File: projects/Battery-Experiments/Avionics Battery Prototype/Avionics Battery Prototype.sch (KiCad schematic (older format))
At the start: 21 parts, among them U1 LM324A

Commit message: AVB Start
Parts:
- removed U1: LM324A, symbol Amplifier_Operational:LM324A
- added C1, C2, C3, C4: 0.1u, Capacitors_SMD:C_1206_HandSoldering, symbol Device:C
- added C5, C6: 1u, Capacitors_SMD:C_1206_HandSoldering, symbol Device:C
- added C7, C9: 10n, Capacitors_SMD:C_1206_HandSoldering, symbol Device:C
- added C8: 10u, Capacitors_SMD:C_1206_HandSoldering, symbol Device:C
- added D1, D2, D3, D4: 3.6V Zener, Diodes_SMD:D_SOD-123F, symbol Device:D_Zener_ALT
- added D5, D6: LED, LEDs:LED_1206_HandSoldering, symbol Device:LED_ALT
- added J1: Jack-DC, Connect:Banana_Jack_2Pin, symbol Connector:Jack-DC
- added J2: TP, Pin_Headers:Pin_Header_Straight_1x02_Pitch2.54mm, symbol Connector_Generic:Conn_01x02
- added J3: UART, Pin_Headers:Pin_Header_Straight_1x03_Pitch2.54mm, symbol Connector_Generic:Conn_01x03
- added J4: SBW JTAG, Pin_Headers:Pin_Header_Straight_1x06_Pitch2.54mm, symbol Connector_Generic:Conn_01x06
- added R10, R15, R20, R23, R24, R5: 330, Resistors_SMD:R_1206_HandSoldering, symbol Device:R
- added R21, R22, R25: 33k, Resistors_SMD:R_1206_HandSoldering, symbol Device:R
- added U1, U2: OPA4197, SMD_Packages:SOIC-14_N, symbol k7arx:OPA4322
- added U3: CD4052B, SMD_Packages:SO-16-N, symbol Analog_Switch:CD4052B
- added U4: LT1763, SMD_Packages:SOIC-8-N, symbol k7arx:LT1763
- added U5: MSP430G2233, SMD_Packages:SSOP-20, symbol k7arx:MSP430G2233
- added U6: CD40109B, SMD_Packages:SO-16-N, symbol k7arx:CD40109B
- BT1, BT2, BT3, BT4: value Battery_Cell -> 14430; footprint (none) -> k7arx:Keystone-92 Battery_Contact 14430
- R1, R2: value 20k -> 200k; footprint (none) -> Resistors_SMD:R_1206_HandSoldering
- R11: renamed from R9; value 20k -> 200k; footprint (none) -> Resistors_SMD:R_1206_HandSoldering
- R12: renamed from R10; value 20k -> 200k; footprint (none) -> Resistors_SMD:R_1206_HandSoldering
- R13: renamed from R11; value 10k -> 100k; footprint (none) -> Resistors_SMD:R_1206_HandSoldering
- R14: renamed from R12; value 10k -> 100k; footprint (none) -> Resistors_SMD:R_1206_HandSoldering
- R16: renamed from R13; value 20k -> 200k; footprint (none) -> Resistors_SMD:R_1206_HandSoldering
- R17: renamed from R14; value 20k -> 200k; footprint (none) -> Resistors_SMD:R_1206_HandSoldering
- R18: renamed from R15; value 10k -> 100k; footprint (none) -> Resistors_SMD:R_1206_HandSoldering
- R19: renamed from R16; value 10k -> 100k; footprint (none) -> Resistors_SMD:R_1206_HandSoldering
- R3, R4: value 10k -> 100k; footprint (none) -> Resistors_SMD:R_1206_HandSoldering
- R6: renamed from R5; value 20k -> 200k; footprint (none) -> Resistors_SMD:R_1206_HandSoldering
- R7: renamed from R6; value 20k -> 200k; footprint (none) -> Resistors_SMD:R_1206_HandSoldering
- R8: renamed from R7; value 10k -> 100k; footprint (none) -> Resistors_SMD:R_1206_HandSoldering
- R9: renamed from R8; value 10k -> 100k; footprint (none) -> Resistors_SMD:R_1206_HandSoldering
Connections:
- net +BATT: now also C6.1, J2.2 (Pin_2), R21.1, U1.10 (+), U1.4 (V+), U2.4 (V+), U3.16 (VDD), U4.5 (~SHDN), U4.8 (VIN), U6.16 (Vdd); no longer BT4.1 (+), R17.2
- net GND: now also C1.2, C2.2, C3.2, C4.2, C6.2, C8.2, C9.2, D1.2 (A), D2.2 (A), D3.2 (A), D4.2 (A), D5.1 (K), D6.1 (K), J1.2, J3.1 (Pin_1), J4.3 (Pin_3), J4.5 (Pin_5), R25.2, U1.11 (V-), U2.11 (V-), U3.1 (Y0), U3.7 (VEE), U3.8 (VSS), U4.3 (GND), U4.6 (GND), U4.7 (GND), U5.14 (P1.6), U5.15 (P1.7), U5.18 (XOut), U5.19 (XIn), U5.20 (DVss), U6.13 (H), U6.14 (D), U6.15 (En_D), U6.8 (Vss)
- net V1: now also C1.1, D1.1 (K), R5.1, U5.2 (P1.0); no longer R3.1
- net V2: now also C2.1, D2.1 (K), R10.1, U5.3 (P1.1); no longer R8.1
- net V3: now also C3.1, D3.1 (K), R15.1, U5.4 (P1.2); no longer R13.1
- net V4: now also C4.1, D4.1 (K), R20.1, U5.5 (P1.3); no longer R18.1
- net at BT3.1 (+), BT4.2 (-): now also U1.12 (+), U3.15 (X2), U3.4 (Y3); no longer R12.2, R16.2
- net at BT2.1 (+), BT3.2 (-): now also U1.5 (+), U3.14 (X1), U3.2 (Y2); no longer R11.2, R7.2
- net at BT1.1 (+), BT2.2 (-): now also U1.3 (+), U3.12 (X0), U3.5 (Y1); no longer R2.2, R6.2
- net at R1.1, R3.2: now also U2.2 (-)
- net at R2.1, R4.2: now also U2.3 (+)
- net at R7.1, R9.2: now also U2.5 (+)
- net at R6.1, R8.2: now also U2.6 (-)
- net at R12.1, R14.2: now also U2.10 (+)
- net at R11.1, R13.2: now also U2.9 (-)
- net at R17.1, R19.2: now also U2.12 (+)
- net at R16.1, R18.2: now also U2.13 (-)
- new net: BT4.1 (+), J1.1, J2.1 (Pin_1), U3.11 (X3)
- new net: R2.2, R6.2, U1.1, U1.2 (-)
- new net: R11.2, R7.2, U1.6 (-), U1.7
- new net: R12.2, R16.2, U1.13 (-), U1.14
- new net: R17.2, U1.8, U1.9 (-)
- new net: C5.1, U3.13 (X)
- new net: C5.2, U3.3 (Y)
- new net: U3.10 (A), U6.4 (E)
- new net: R21.2, U3.6 (INH), U6.11 (G)
- new net: U3.9 (B), U6.5 (F)
- new net: R3.1, R5.2, U2.1
- new net: R10.2, R8.1, U2.7
- new net: R13.1, R15.2, U2.8
- new net: R18.1, R20.2, U2.14
- new net: C7.2, U4.4 (BYP)
- new net: U5.10 (P2.2), U6.10 (C)
- new net: R25.1, U5.11 (P2.3), U6.2 (En_A), U6.7 (En_B), U6.9 (En_C)
- new net: U5.8 (P2.0), U6.3 (A)
- new net: U5.9 (P2.1), U6.6 (B)
- new net: R23.1, U5.6 (P1.4)
- new net: D5.2 (A), R23.2
- new net: R24.1, U5.7 (P1.5)
- new net: D6.2 (A), R24.2
- new net +3V3: C7.1, C8.1, J4.2 (Pin_2), J4.4 (Pin_4), R22.1, U4.1 (VOUT), U4.2 (SENSE), U5.1 (DVcc), U6.1 (Vcc)
- new net TEST: J4.6 (Pin_6), U5.17 (TEST)
- new net UART_RX: J3.2 (Pin_2), U5.12 (P2.4)
- new net UART_TX: J3.3 (Pin_3), U5.13 (P2.5)
- new net ~RST: C9.1, J4.1 (Pin_1), R22.2, U5.16 (~RST)
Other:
- note added: "Battery balancing and monitoring circuit"
- note added: "Battery control system circuit"
- moved on the sheet: BT1, BT2, BT3, BT4, R1, R11, R12, R13, R14, R16, R17, R18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

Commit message: AVB Rev B Complete
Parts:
- added S1: Power Switch, k7arx:PB400 DPST Pushbutton Switch, symbol k7arx:DPST_PowerSwitch
- added S2: Tac Switch, k7arx:EVQ2_Momentary_Switch, symbol k7arx:TactileSwitch_NO
- added TP1: 3V3, Pin_Headers:Pin_Header_Straight_1x01_Pitch2.54mm, symbol Connector:Conn_01x01_Female
- added TP2: Gnd, Pin_Headers:Pin_Header_Straight_1x01_Pitch2.54mm, symbol Connector:Conn_01x01_Female
- J2: value TP -> Enable
- J4: footprint Pin_Headers:Pin_Header_Straight_1x06_Pitch2.54mm -> k7arx:Tag-Connect_TC2030-NL
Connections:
- net +3V3: now also TP1.1 (Pin_1)
- net GND: now also S2.2 (COM), TP2.1 (Pin_1)
- net ~RST: now also S2.1 (NO)
- net at BT4.1 (+), U3.11 (X3): now also S1.2 (COM1), S1.4 (COM2); no longer J1.1, J2.1 (Pin_1)
- new net: J1.1, J2.1 (Pin_1), S1.1 (NO1), S1.3 (NO2)
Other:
- moved on the sheet: C9, J1, J2, R22
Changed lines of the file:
@@
 L Device:R R22
 U 1 1 605F86BF
-P 3650 2750
-F 0 "R22" H 3720 2796 50  0000 L CNN
-F 1 "33k" V 3650 2675 50  0000 L CNN
-F 2 "Resistors_SMD:R_1206_HandSoldering" V 3580 2750 50  0001 C CNN
-F 3 "~" H 3650 2750 50  0001 C CNN
-	1    3650 2750
+P 3350 2750
+F 0 "R22" H 3420 2796 50  0000 L CNN
+F 1 "33k" V 3350 2675 50  0000 L CNN
+F 2 "Resistors_SMD:R_1206_HandSoldering" V 3280 2750 50  0001 C CNN
+F 3 "~" H 3350 2750 50  0001 C CNN
+	1    3350 2750
 	1    0    0    -1
 $EndComp
@@
 L Device:C C9
 U 1 1 605F8EF7
-P 3650 3250
-F 0 "C9" H 3765 3296 50  0000 L CNN
-F 1 "10n" H 3765 3205 50  0000 L CNN
-F 2 "Capacitors_SMD:C_1206_HandSoldering" H 3688 3100 50  0001 C CNN
-F 3 "~" H 3650 3250 50  0001 C CNN
-	1    3650 3250
+P 3350 3250
+F 0 "C9" H 3465 3296 50  0000 L CNN
+F 1 "10n" H 3465 3205 50  0000 L CNN
+F 2 "Capacitors_SMD:C_1206_HandSoldering" H 3388 3100 50  0001 C CNN
+F 3 "~" H 3350 3250 50  0001 C CNN
+	1    3350 3250
 	1    0    0    -1
 $EndComp
@@
 L power:GND #PWR0118
 U 1 1 605F9538
-P 3650 3450
-F 0 "#PWR0118" H 3650 3200 50  0001 C CNN
-F 1 "GND" H 3650 3300 50  0000 C CNN
-F 2 "" H 3650 3450 50  0001 C CNN
-F 3 "" H 3650 3450 50  0001 C CNN
-	1    3650 3450
-	1    0    0    -1
-$EndComp
-Text GLabel 3750 3000 2    50   Input ~ 0
+P 3350 3450
+F 0 "#PWR0118" H 3350 3200 50  0001 C CNN
+F 1 "GND" H 3350 3300 50  0000 C CNN
+F 2 "" H 3350 3450 50  0001 C CNN
+F 3 "" H 3350 3450 50  0001 C CNN
+	1    3350 3450
+	1    0    0    -1
+$EndComp
+Text GLabel 3900 3000 2    50   Input ~ 0
 ~RST
 Text GLabel 2850 2900 2    50   Input ~ 0
@@
 L Connector:Jack-DC J1
 U 1 1 6078A590
-P 6050 1200
-F 0 "J1" H 6107 1525 50  0000 C CNN
-F 1 "Jack-DC" H 6107 1434 50  0000 C CNN
-F 2 "Connect:Banana_Jack_2Pin" H 6100 1160 50  0001 C CNN
-F 3 "~" H 6100 1160 50  0001 C CNN
-	1    6050 1200
+P 5700 1200
+F 0 "J1" H 5757 1525 50  0000 C CNN
+F 1 "Jack-DC" H 5757 1434 50  0000 C CNN
+F 2 "Connect:Banana_Jack_2Pin" H 5750 1160 50  0001 C CNN
+F 3 "~" H 5750 1160 50  0001 C CNN
+	1    5700 1200
 	1    0    0    -1
 $EndComp
@@
 L power:GND #PWR0124
 U 1 1 607952FC
-P 6400 1350
-F 0 "#PWR0124" H 6400 1100 50  0001 C CNN
-F 1 "GND" H 6400 1200 50  0000 C CNN
-F 2 "" H 6400 1350 50  0001 C CNN
-F 3 "" H 6400 1350 50  0001 C CNN
-	1    6400 1350
+P 6050 1350
+F 0 "#PWR0124" H 6050 1100 50  0001 C CNN
+F 1 "GND" H 6050 1200 50  0000 C CNN
+F 2 "" H 6050 1350 50  0001 C CNN
+F 3 "" H 6050 1350 50  0001 C CNN
+	1    6050 1350
 	1    0    0    -1
 $EndComp
@@
 F 0 "J4" H 1618 5275 50  0000 C CNN
 F 1 "SBW JTAG" H 1618 5366 50  0000 C CNN
-F 2 "Pin_Headers:Pin_Header_Straight_1x06_Pitch2.54mm" H 1700 5800 50  0001 C CNN
+F 2 "k7arx:Tag-Connect_TC2030-NL" H 1700 5800 50  0001 C CNN
 F 3 "~" H 1700 5800 50  0001 C CNN
 	1    1700 5800
@@
 L power:+3V3 #PWR0133
 U 1 1 606E803F
-P 3650 2500
-F 0 "#PWR0133" H 3650 2350 50  0001 C CNN
-F 1 "+3V3" H 3650 2650 50  0000 C CNN
-F 2 "" H 3650 2500 50  0001 C CNN
-F 3 "" H 3650 2500 50  0001 C CNN
-	1    3650 2500
+P 3350 2500
+F 0 "#PWR0133" H 3350 2350 50  0001 C CNN
+F 1 "+3V3" H 3350 2650 50  0000 C CNN
+F 2 "" H 3350 2500 50  0001 C CNN
+F 3 "" H 3350 2500 50  0001 C CNN
+	1    3350 2500
 	1    0    0    -1
 $EndComp
@@
 	2800 3400 2850 3400
 Wire Wire Line
-	3650 3450 3650 3400
-Wire Wire Line
-	3650 3100 3650 3000
-Wire Wire Line
-	3750 3000 3650 3000
-Connection ~ 3650 3000
-Wire Wire Line
-	3650 3000 3650 2900
-Wire Wire Line
-	3650 2600 3650 2500
+	3350 3450 3350 3400
+Wire Wire Line
+	3350 3100 3350 3000
+Connection ~ 3350 3000
+Wire Wire Line
+	3350 3000 3350 2900
+Wire Wire Line
+	3350 2600 3350 2500
 Wire Wire Line
 	2800 3300 2850 3300
@@
 Wire Wire Line
 	1050 3850 1050 3900
-Wire Wire Line
-	2800 3000 3650 3000
 Wire Wire Line
 	1700 3300 1700 4550
@@
 Wire Notes Line width 32 style solid rgb(214, 0, 0)
 	7350 1200 7150 1200
-Wire Wire Line
-	7250 1100 6350 1100
-Wire Wire Line
-	6350 1300 6400 1300
-Wire Wire Line
-	6400 1300 6400 1350
 Wire Notes Line width 32 style solid rgb(214, 0, 0)
 	7350 5200 7150 5200
@@
 L Connector_Generic:Conn_01x02 J2
 U 1 1 610EB4DA
-P 7050 1000
-F 0 "J2" V 7250 950 50  0000 C CNN
-F 1 "TP" V 7150 950 50  0000 C CNN
-F 2 "Pin_Headers:Pin_Header_Straight_1x02_Pitch2.54mm" H 7050 1000 50  0001 C CNN
-F 3 "~" H 7050 1000 50  0001 C CNN
-	1    7050 1000
+P 6250 1000
+F 0 "J2" V 6450 950 50  0000 C CNN
+F 1 "Enable" V 6350 950 50  0000 C CNN
+F 2 "Pin_Headers:Pin_Header_Straight_1x02_Pitch2.54mm" H 6250 1000 50  0001 C CNN
+F 3 "~" H 6250 1000 50  0001 C CNN
+	1    6250 1000
 	-1   0    0    1
 $EndComp
-Wire Wire Line
-	7250 1000 7250 1100
-Connection ~ 7250 1100
 Wire Wire Line
 	7250 900  7250 850
@@
 Wire Wire Line
 	7400 900  7250 900
-Connection ~ 7250 900
 Wire Wire Line
 	7050 4800 7050 4550
@@
 	7050 4550 7250 4550
 Connection ~ 7250 4550
+Wire Wire Line
+	2800 3000 3350 3000
+$Comp
+L k7arx:TactileSwitch_NO S2
+U 1 1 6050288C
+P 3700 3250
+F 0 "S2" V 3647 3418 60  0000 L CNN
+F 1 "Tac Switch" V 3753 3418 60  0000 L CNN
+F 2 "k7arx:EVQ2_Momentary_Switch" H 3700 3250 60  0001 C CNN
+F 3 "" H 3700 3250 60  0001 C CNN
+	1    3700 3250
+	0    1    1    0
+$EndComp
+$Comp
+L power:GND #PWR0141
+U 1 1 605034C9
+P 3700 3450
+F 0 "#PWR0141" H 3700 3200 50  0001 C CNN
+F 1 "GND" H 3700 3300 50  0000 C CNN
+F 2 "" H 3700 3450 50  0001 C CNN
+F 3 "" H 3700 3450 50  0001 C CNN
+	1    3700 3450
+	1    0    0    -1
+$EndComp
+Wire Wire Line
+	3700 3000 3700 3050
+Wire Wire Line
+	3350 3000 3700 3000
+Wire Wire Line
+	3700 3000 3900 3000
+Connection ~ 3700 3000
+$Comp
+L k7arx:DPST_PowerSwitch S1
+U 1 1 6057BD9E
+P 6750 1150
+F 0 "S1" H 6750 1300 60  0000 C CNN
+F 1 "Power Switch" H 6750 1000 60  0000 C CNN
+F 2 "k7arx:PB400 DPST Pushbutton Switch" H 6750 1100 60  0001 C CNN
+F 3 "" H 6750 1100 60  0001 C CNN
+	1    6750 1150
+	1    0    0    -1
+$EndComp
+Wire Wire Line
+	7250 1100 6950 1100
+Wire Wire Line
+	6950 1200 6950 1100
+Wire Wire Line
+	6550 1100 6450 1100
+Wire Wire Line
+	6550 1200 6550 1100
+Wire Wire Line
+	6450 1000 6450 1100
+Connection ~ 6450 1100
+Wire Wire Line
+	6450 1100 6000 1100
+Wire Wire Line
+	6450 900  7250 900
+Connection ~ 7250 900
+Wire Wire Line
+	6000 1300 6050 1300
+Wire Wire Line
+	6050 1300 6050 1350
+Connection ~ 6550 1100
+Connection ~ 6950 1100
+$Comp
+L Connector:Conn_01x01_Female TP1
+U 1 1 606D70AF
+P 3750 1200
+F 0 "TP1" H 3778 1226 50  0000 L CNN
+F 1 "3V3" H 3778 1135 50  0000 L CNN
+F 2 "Pin_Headers:Pin_Header_Straight_1x01_Pitch2.54mm" H 3750 1200 50  0001 C CNN
+F 3 "~" H 3750 1200 50  0001 C CNN
+	1    3750 1200
+	1    0    0    -1
+$EndComp
+$Comp
+L Connector:Conn_01x01_Female TP2
+U 1 1 606D87ED
+P 3750 1500
+F 0 "TP2" H 3778 1526 50  0000 L CNN
+F 1 "Gnd" H 3778 1435 50  0000 L CNN
+F 2 "Pin_Headers:Pin_Header_Straight_1x01_Pitch2.54mm" H 3750 1500 50  0001 C CNN
+F 3 "~" H 3750 1500 50  0001 C CNN
+	1    3750 1500
+	1    0    0    -1
+$EndComp
+Wire Wire Line
+	3250 1200 3550 1200
+Connection ~ 3250 1200
+Wire Wire Line
+	3250 1500 3550 1500
+Connection ~ 3250 1500
 $EndSCHEMATC

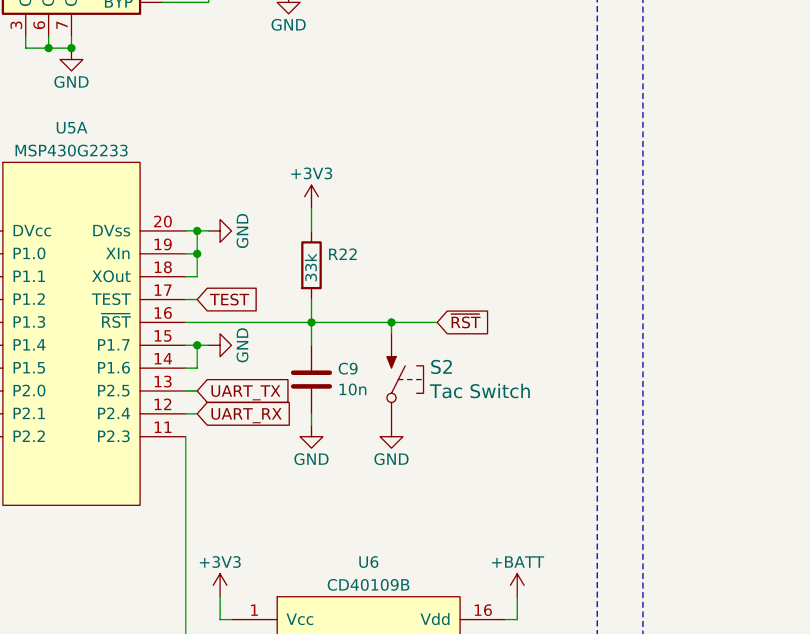
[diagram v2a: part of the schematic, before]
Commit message: AVB add Xtal tp to uc
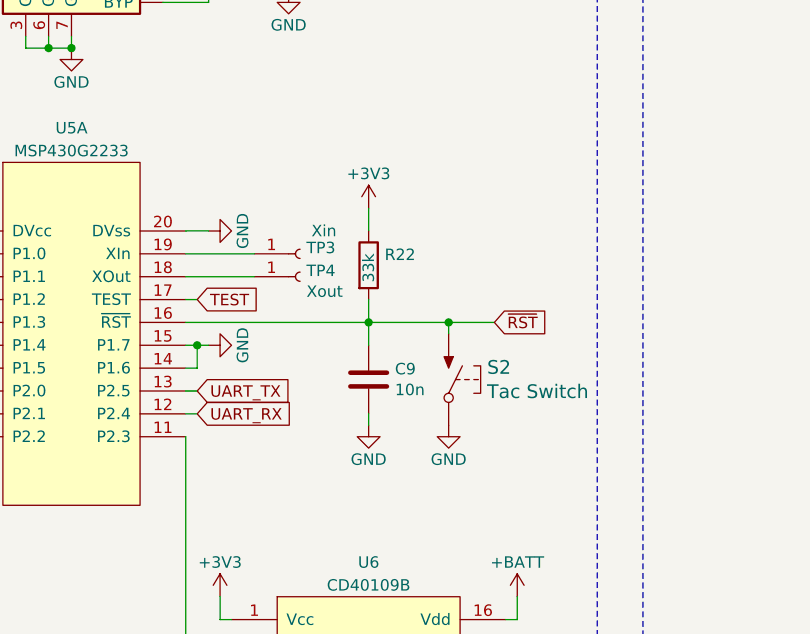
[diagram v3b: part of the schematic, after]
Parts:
- added TP3: Xin, Pin_Headers:Pin_Header_Straight_1x01_Pitch2.54mm, symbol Connector:Conn_01x01_Female
- added TP4: Xout, Pin_Headers:Pin_Header_Straight_1x01_Pitch2.54mm, symbol Connector:Conn_01x01_Female
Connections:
- net GND: no longer U5.18 (XOut), U5.19 (XIn)
- new net: TP3.1 (Pin_1), U5.19 (XIn)
- new net: TP4.1 (Pin_1), U5.18 (XOut)
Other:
- moved on the sheet: C9, R22, S2
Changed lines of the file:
@@
 L Device:R R22
 U 1 1 605F86BF
-P 3350 2750
-F 0 "R22" H 3420 2796 50  0000 L CNN
-F 1 "33k" V 3350 2675 50  0000 L CNN
-F 2 "Resistors_SMD:R_1206_HandSoldering" V 3280 2750 50  0001 C CNN
-F 3 "~" H 3350 2750 50  0001 C CNN
-	1    3350 2750
+P 3600 2750
+F 0 "R22" H 3670 2796 50  0000 L CNN
+F 1 "33k" V 3600 2675 50  0000 L CNN
+F 2 "Resistors_SMD:R_1206_HandSoldering" V 3530 2750 50  0001 C CNN
+F 3 "~" H 3600 2750 50  0001 C CNN
+	1    3600 2750
 	1    0    0    -1
 $EndComp
@@
 L Device:C C9
 U 1 1 605F8EF7
-P 3350 3250
-F 0 "C9" H 3465 3296 50  0000 L CNN
-F 1 "10n" H 3465 3205 50  0000 L CNN
-F 2 "Capacitors_SMD:C_1206_HandSoldering" H 3388 3100 50  0001 C CNN
-F 3 "~" H 3350 3250 50  0001 C CNN
-	1    3350 3250
+P 3600 3250
+F 0 "C9" H 3715 3296 50  0000 L CNN
+F 1 "10n" H 3715 3205 50  0000 L CNN
+F 2 "Capacitors_SMD:C_1206_HandSoldering" H 3638 3100 50  0001 C CNN
+F 3 "~" H 3600 3250 50  0001 C CNN
+	1    3600 3250
 	1    0    0    -1
 $EndComp
@@
 L power:GND #PWR0118
 U 1 1 605F9538
-P 3350 3450
-F 0 "#PWR0118" H 3350 3200 50  0001 C CNN
-F 1 "GND" H 3350 3300 50  0000 C CNN
-F 2 "" H 3350 3450 50  0001 C CNN
-F 3 "" H 3350 3450 50  0001 C CNN
-	1    3350 3450
-	1    0    0    -1
-$EndComp
-Text GLabel 3900 3000 2    50   Input ~ 0
+P 3600 3450
+F 0 "#PWR0118" H 3600 3200 50  0001 C CNN
+F 1 "GND" H 3600 3300 50  0000 C CNN
+F 2 "" H 3600 3450 50  0001 C CNN
+F 3 "" H 3600 3450 50  0001 C CNN
+	1    3600 3450
+	1    0    0    -1
+$EndComp
+Text GLabel 4150 3000 2    50   Input ~ 0
 ~RST
 Text GLabel 2850 2900 2    50   Input ~ 0
@@
 L power:+3V3 #PWR0133
 U 1 1 606E803F
-P 3350 2500
-F 0 "#PWR0133" H 3350 2350 50  0001 C CNN
-F 1 "+3V3" H 3350 2650 50  0000 C CNN
-F 2 "" H 3350 2500 50  0001 C CNN
-F 3 "" H 3350 2500 50  0001 C CNN
-	1    3350 2500
+P 3600 2500
+F 0 "#PWR0133" H 3600 2350 50  0001 C CNN
+F 1 "+3V3" H 3600 2650 50  0000 C CNN
+F 2 "" H 3600 2500 50  0001 C CNN
+F 3 "" H 3600 2500 50  0001 C CNN
+	1    3600 2500
 	1    0    0    -1
 $EndComp
@@
 	2800 2900 2850 2900
 Wire Wire Line
-	2800 2600 2850 2600
-Wire Wire Line
 	2800 3400 2850 3400
 Wire Wire Line
-	3350 3450 3350 3400
-Wire Wire Line
-	3350 3100 3350 3000
-Connection ~ 3350 3000
-Wire Wire Line
-	3350 3000 3350 2900
-Wire Wire Line
-	3350 2600 3350 2500
+	3600 3450 3600 3400
+Wire Wire Line
+	3600 3100 3600 3000
+Connection ~ 3600 3000
+Wire Wire Line
+	3600 3000 3600 2900
+Wire Wire Line
+	3600 2600 3600 2500
 Wire Wire Line
 	2800 3300 2850 3300
@@
 Wire Wire Line
 	1700 2500 1700 2600
-Wire Wire Line
-	2800 2700 2850 2700
-Wire Wire Line
-	2850 2700 2850 2600
-Connection ~ 2850 2600
-Wire Wire Line
-	2850 2600 2900 2600
-Wire Wire Line
-	2800 2800 2850 2800
-Wire Wire Line
-	2850 2800 2850 2700
-Connection ~ 2850 2700
 Wire Wire Line
 	2950 4200 2950 4300
@@
 	7050 4550 7250 4550
 Connection ~ 7250 4550
-Wire Wire Line
-	2800 3000 3350 3000
 $Comp
 L k7arx:TactileSwitch_NO S2
 U 1 1 6050288C
-P 3700 3250
-F 0 "S2" V 3647 3418 60  0000 L CNN
-F 1 "Tac Switch" V 3753 3418 60  0000 L CNN
-F 2 "k7arx:EVQ2_Momentary_Switch" H 3700 3250 60  0001 C CNN
-F 3 "" H 3700 3250 60  0001 C CNN
-	1    3700 3250
+P 3950 3250
+F 0 "S2" V 3897 3418 60  0000 L CNN
+F 1 "Tac Switch" V 4003 3418 60  0000 L CNN
+F 2 "k7arx:EVQ2_Momentary_Switch" H 3950 3250 60  0001 C CNN
+F 3 "" H 3950 3250 60  0001 C CNN
+	1    3950 3250
 	0    1    1    0
 $EndComp
@@
 L power:GND #PWR0141
 U 1 1 605034C9
-P 3700 3450
-F 0 "#PWR0141" H 3700 3200 50  0001 C CNN
-F 1 "GND" H 3700 3300 50  0000 C CNN
-F 2 "" H 3700 3450 50  0001 C CNN
-F 3 "" H 3700 3450 50  0001 C CNN
-	1    3700 3450
-	1    0    0    -1
-$EndComp
-Wire Wire Line
-	3700 3000 3700 3050
-Wire Wire Line
-	3350 3000 3700 3000
-Wire Wire Line
-	3700 3000 3900 3000
-Connection ~ 3700 3000
+P 3950 3450
+F 0 "#PWR0141" H 3950 3200 50  0001 C CNN
+F 1 "GND" H 3950 3300 50  0000 C CNN
+F 2 "" H 3950 3450 50  0001 C CNN
+F 3 "" H 3950 3450 50  0001 C CNN
+	1    3950 3450
+	1    0    0    -1
+$EndComp
+Wire Wire Line
+	3950 3000 3950 3050
+Wire Wire Line
+	3600 3000 3950 3000
+Wire Wire Line
+	3950 3000 4150 3000
+Connection ~ 3950 3000
 $Comp
 L k7arx:DPST_PowerSwitch S1
@@
 	3250 1500 3550 1500
 Connection ~ 3250 1500
+Wire Wire Line
+	2800 2600 2900 2600
+$Comp
+L Connector:Conn_01x01_Female TP3
+U 1 1 6061AE7F
+P 3300 2700
+F 0 "TP3" H 3328 2726 50  0000 L CNN
+F 1 "Xin" H 3350 2800 50  0000 L CNN
+F 2 "Pin_Headers:Pin_Header_Straight_1x01_Pitch2.54mm" H 3300 2700 50  0001 C CNN
+F 3 "~" H 3300 2700 50  0001 C CNN
+	1    3300 2700
+	1    0    0    -1
+$EndComp
+$Comp
+L Connector:Conn_01x01_Female TP4
+U 1 1 6061B8E9
+P 3300 2800
+F 0 "TP4" H 3328 2826 50  0000 L CNN
+F 1 "Xout" H 3328 2735 50  0000 L CNN
+F 2 "Pin_Headers:Pin_Header_Straight_1x01_Pitch2.54mm" H 3300 2800 50  0001 C CNN
+F 3 "~" H 3300 2800 50  0001 C CNN
+	1    3300 2800
+	1    0    0    -1
+$EndComp
+Wire Wire Line
+	2800 3000 3600 3000
+Wire Wire Line
+	2800 2700 3100 2700
+Wire Wire Line
+	2800 2800 3100 2800
 $EndSCHEMATC
